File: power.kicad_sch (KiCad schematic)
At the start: 33 parts, among them J7 USB-C_GCT_USB4105-GF-A, J8 Molex_Nano-Fit_1x2_SMD_105430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, U10 TPS564247DRLR, U6 TPS564247DRLR, U7 TPS564247DRLR, U8 TPS564247DRLR, U9 TPS564247DRLR

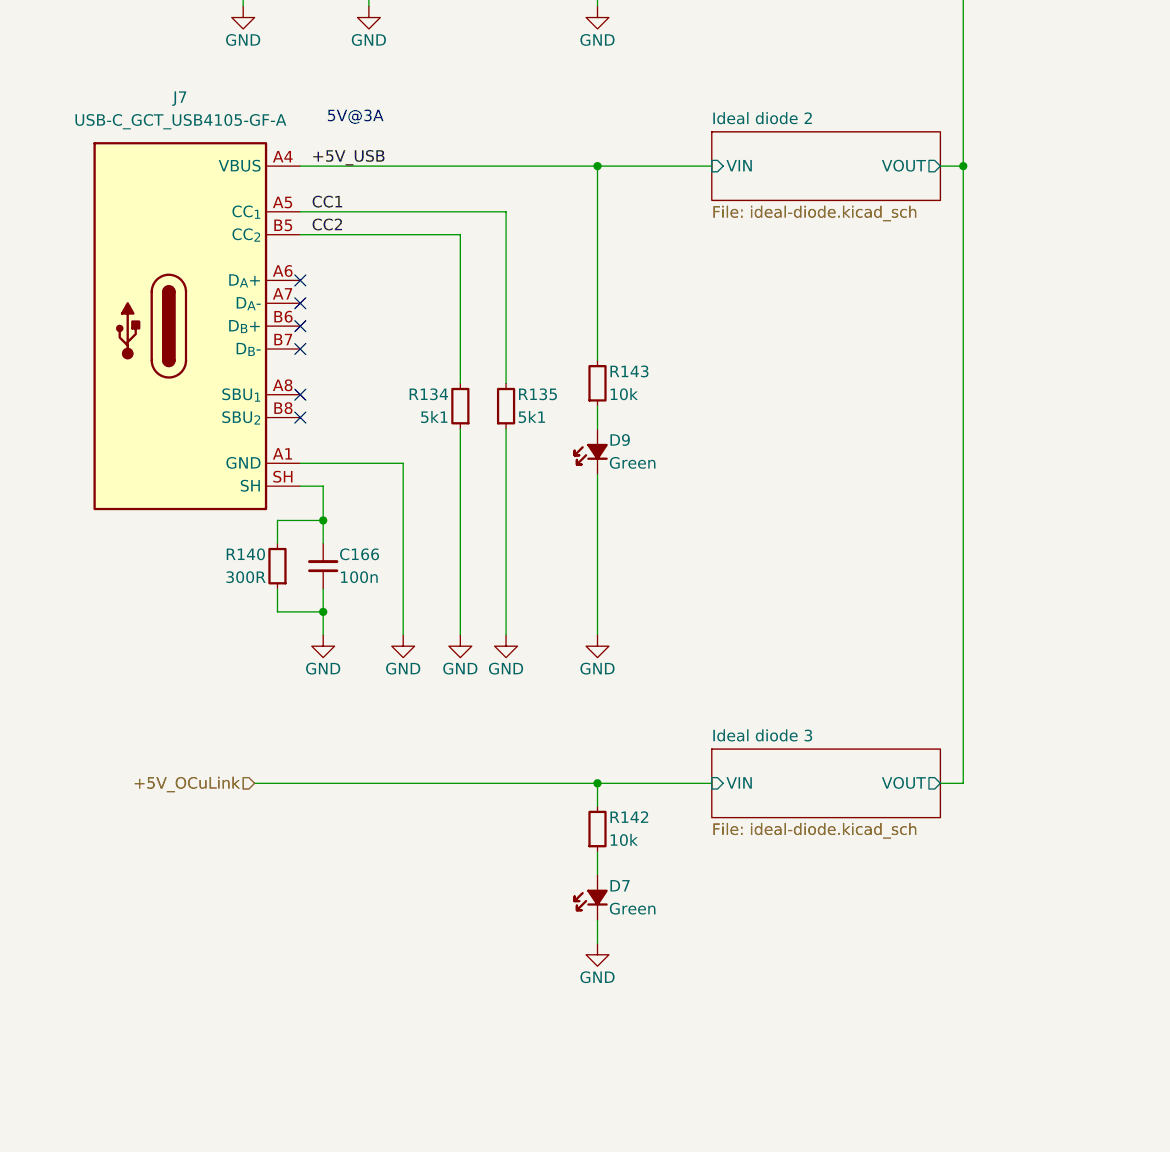
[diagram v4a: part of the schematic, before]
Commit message: [#80813] Remove OCuLink power pins connections
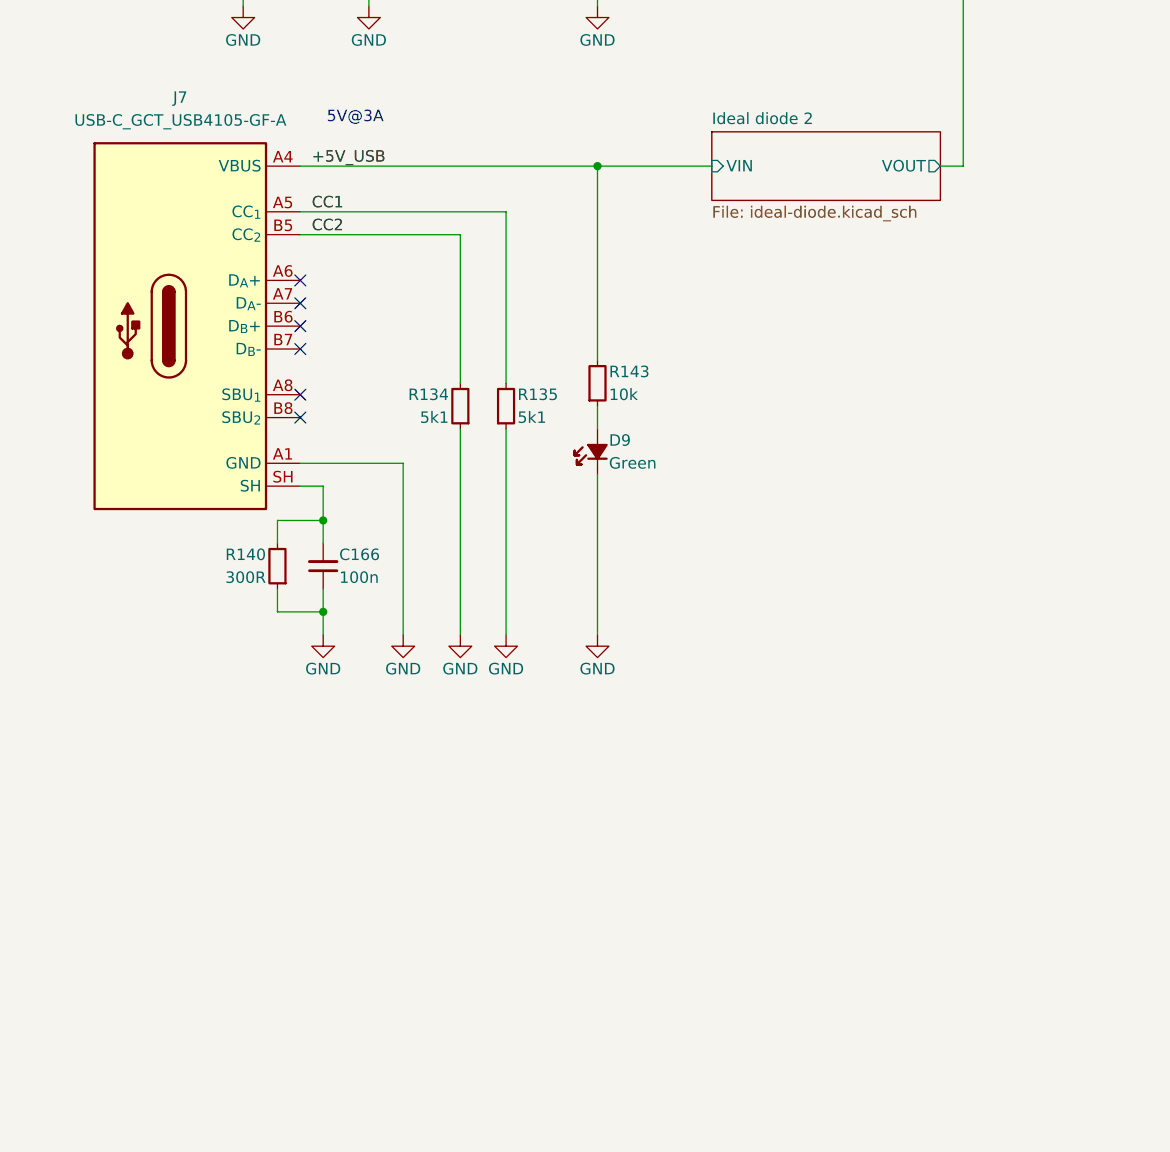
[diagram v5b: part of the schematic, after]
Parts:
- removed D7: LED_G_0603_LG_L29K-G2J1-24-Z, antmicro-footprints:LED_0603_1608Metric_G, symbol antmicroLEDIndicationDiscrete:LED_G_0603_LG_L29K-G2J1-24-Z
- removed R142: R_10k_0402, antmicro-footprints:R_0402_1005Metric, symbol antmicroResistors0402:R_10k_0402
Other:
- removed sheet Ideal diode 3

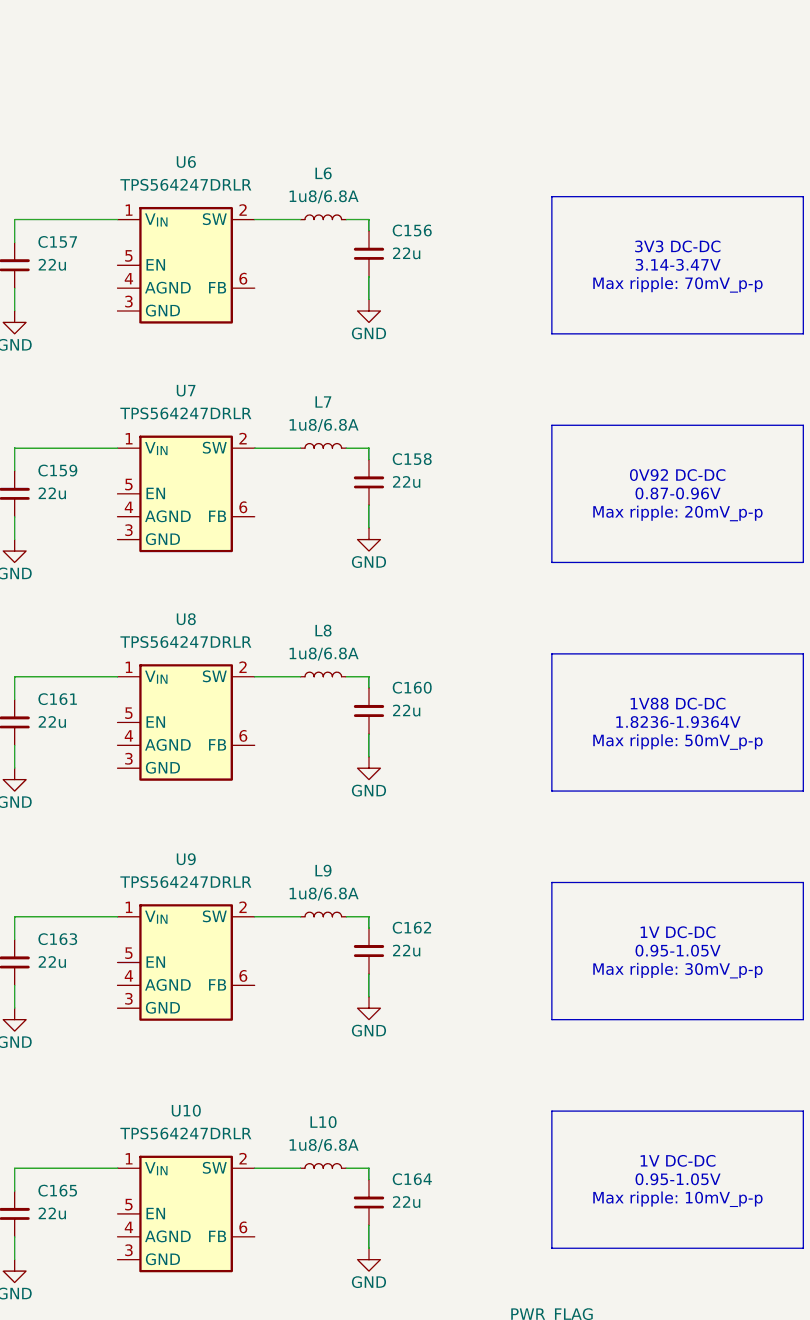
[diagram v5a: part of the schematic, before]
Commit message: [#80813] Change inductors, minor PCB changes
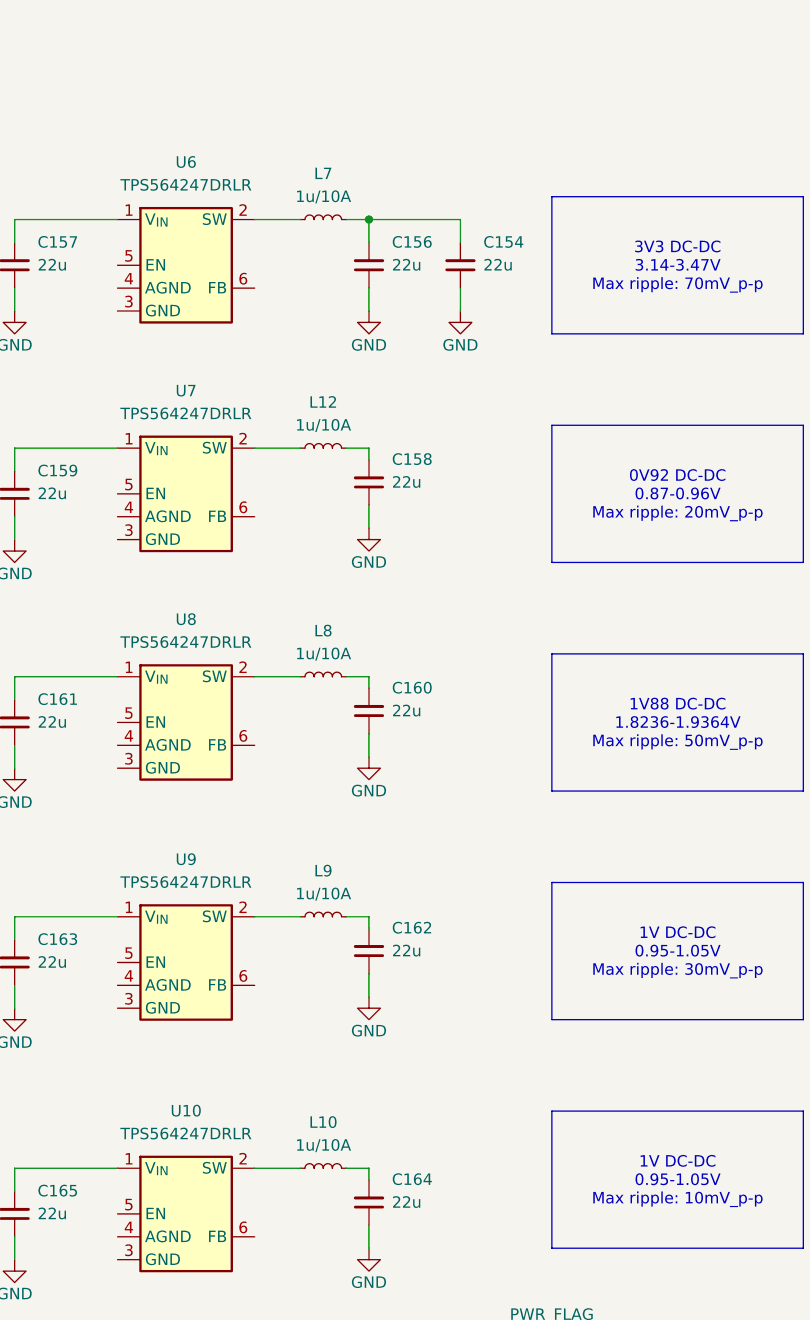
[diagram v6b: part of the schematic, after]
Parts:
- removed L10, L6, L7, L8, L9: L_1u8_6.8A_WE-MAPI-4020, antmicro-footprints:L_WE-MAPI-4020, symbol antmicroFixedInductors:L_1u8_6.8A_WE-MAPI-4020
- added C154: C_22u_16V_0603, antmicro-footprints:C_0603_1608Metric, symbol antmicroCapacitors0603:C_22u_16V_0603
- added L10, L12, L7, L8, L9: L_1u_10A_Bourns-SRP4021HMT, antmicro-footprints:L_Bourns-SRP4021HMT, symbol antmicroFixedInductors:L_1u_10A_Bourns-SRP4021HMT
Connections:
- net GND: now also C154.1
- net at C156.2: now also C154.2, L7.2
- net at C162.2: now also L9.2
- net at U10.2 (SW): now also L10.1
- net at U8.2 (SW): now also L8.1
- net at C160.2: now also L8.2
- net at U6.2 (SW): now also L7.1
- net at U7.2 (SW): now also L12.1
- net at U9.2 (SW): now also L9.1
- net at C158.2: now also L12.2
- net at C164.2: now also L10.2
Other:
- moved on the sheet: C156

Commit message: [#81595] Update symbols from library
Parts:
- C154, C156, C157, C158, C159, C160, C161, C162, C163, C164, C165: footprint antmicro-footprints:C_0603_1608Metric -> antmicro-footprints:C_0603_1608Metric_EIA
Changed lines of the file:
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@@
 			)
 		)
-		(property "Footprint" "antmicro-footprints:C_0603_1608Metric"
+		(property "Footprint" "antmicro-footprints:C_0603_1608Metric_EIA"
 			(at 309.88 82.55 0)
 			(effects
@@
 			)
 		)
-		(property "Description" ""
+		(property "Description" "SMD Multilayer Ceramic Capacitor"
 			(at 297.18 102.87 0)
 			(effects
@@
 			)
 		)
-		(property "Footprint" "antmicro-footprints:C_0603_1608Metric"
+		(property "Footprint" "antmicro-footprints:C_0603_1608Metric_EIA"
 			(at 309.88 158.75 0)
 			(effects
@@
 			)
 		)
-		(property "Description" ""
+		(property "Description" "SMD Multilayer Ceramic Capacitor"
 			(at 297.18 179.07 0)
 			(effects
@@
 			)
 		)
-		(property "Datasheet" "https://www.mouser.pl/datasheet/2/54/Bourns_04_01_2025_SRP4021HMT_Datasheet-3580094.pdf"
+		(property "Datasheet" "https://www.mouser.com/datasheet/2/54/Bourns_04_01_2025_SRP4021HMT_Datasheet-3580094.pdf"
 			(at 304.8 187.96 0)
 			(effects
@@
 			)
 		)
-		(property "Datasheet" "https://www.mouser.pl/datasheet/2/54/Bourns_04_01_2025_SRP4021HMT_Datasheet-3580094.pdf"
+		(property "Datasheet" "https://www.mouser.com/datasheet/2/54/Bourns_04_01_2025_SRP4021HMT_Datasheet-3580094.pdf"
 			(at 304.8 161.29 0)
 			(effects
@@
 			)
 		)
-		(property "Datasheet" "https://www.mouser.pl/datasheet/2/54/Bourns_04_01_2025_SRP4021HMT_Datasheet-3580094.pdf"
+		(property "Datasheet" "https://www.mouser.com/datasheet/2/54/Bourns_04_01_2025_SRP4021HMT_Datasheet-3580094.pdf"
 			(at 304.8 215.9 0)
 			(effects
@@
 			)
 		)
-		(property "Datasheet" "https://www.mouser.pl/datasheet/2/54/Bourns_04_01_2025_SRP4021HMT_Datasheet-3580094.pdf"
+		(property "Datasheet" "https://www.mouser.com/datasheet/2/54/Bourns_04_01_2025_SRP4021HMT_Datasheet-3580094.pdf"
 			(at 304.8 135.89 0)
 			(effects
@@
 			)
 		)
-		(property "Footprint" "antmicro-footprints:C_0603_1608Metric"
+		(property "Footprint" "antmicro-footprints:C_0603_1608Metric_EIA"
 			(at 309.88 132.08 0)
 			(effects
@@
 			)
 		)
-		(property "Description" ""
+		(property "Description" "SMD Multilayer Ceramic Capacitor"
 			(at 297.18 152.4 0)
 			(effects
@@
 			)
 		)
-		(property "Footprint" "antmicro-footprints:C_0603_1608Metric"
+		(property "Footprint" "antmicro-footprints:C_0603_1608Metric_EIA"
 			(at 270.51 107.95 0)
 			(effects
@@
 			)
 		)
-		(property "Description" ""
+		(property "Description" "SMD Multilayer Ceramic Capacitor"
 			(at 257.81 128.27 0)
 			(effects
@@
 			)
 		)
-		(property "Footprint" "antmicro-footprints:C_0603_1608Metric"
+		(property "Footprint" "antmicro-footprints:C_0603_1608Metric_EIA"
 			(at 270.51 187.96 0)
 			(effects
@@
 			)
 		)
-		(property "Description" ""
+		(property "Description" "SMD Multilayer Ceramic Capacitor"
 			(at 257.81 208.28 0)
 			(effects
@@
 			)
 		)
-		(property "Footprint" "antmicro-footprints:C_0603_1608Metric"
+		(property "Footprint" "antmicro-footprints:C_0603_1608Metric_EIA"
 			(at 270.51 133.35 0)
 			(effects
@@
 			)
 		)
-		(property "Description" ""
+		(property "Description" "SMD Multilayer Ceramic Capacitor"
 			(at 257.81 153.67 0)
 			(effects
@@
 			)
 		)
-		(property "Footprint" "antmicro-footprints:C_0603_1608Metric"
+		(property "Footprint" "antmicro-footprints:C_0603_1608Metric_EIA"
 			(at 270.51 82.55 0)
 			(effects
@@
 			)
 		)
-		(property "Description" ""
+		(property "Description" "SMD Multilayer Ceramic Capacitor"
 			(at 257.81 102.87 0)
 			(effects
@@
 			)
 		)
-		(property "Footprint" "antmicro-footprints:C_0603_1608Metric"
+		(property "Footprint" "antmicro-footprints:C_0603_1608Metric_EIA"
 			(at 320.04 82.55 0)
 			(effects
@@
 			)
 		)
-		(property "Description" ""
+		(property "Description" "SMD Multilayer Ceramic Capacitor"
 			(at 307.34 102.87 0)
 			(effects
@@
 			)
 		)
-		(property "Footprint" "antmicro-footprints:C_0603_1608Metric"
+		(property "Footprint" "antmicro-footprints:C_0603_1608Metric_EIA"
 			(at 270.51 160.02 0)
 			(effects
@@
 			)
 		)
-		(property "Description" ""
+		(property "Description" "SMD Multilayer Ceramic Capacitor"
 			(at 257.81 180.34 0)
 			(effects
@@
 			)
 		)
-		(property "Footprint" "antmicro-footprints:C_0603_1608Metric"
+		(property "Footprint" "antmicro-footprints:C_0603_1608Metric_EIA"
 			(at 309.88 106.68 0)
 			(effects
@@
 			)
 		)
-		(property "Description" ""
+		(property "Description" "SMD Multilayer Ceramic Capacitor"
 			(at 297.18 127 0)
 			(effects
@@
 			)
 		)
-		(property "Datasheet" "https://www.mouser.pl/datasheet/2/54/Bourns_04_01_2025_SRP4021HMT_Datasheet-3580094.pdf"
+		(property "Datasheet" "https://www.mouser.com/datasheet/2/54/Bourns_04_01_2025_SRP4021HMT_Datasheet-3580094.pdf"
 			(at 304.8 110.49 0)
 			(effects
@@
 			)
 		)
-		(property "Footprint" "antmicro-footprints:C_0603_1608Metric"
+		(property "Footprint" "antmicro-footprints:C_0603_1608Metric_EIA"
 			(at 309.88 186.69 0)
 			(effects
@@
 			)
 		)
-		(property "Description" ""
+		(property "Description" "SMD Multilayer Ceramic Capacitor"
 			(at 297.18 207.01 0)
 			(effects
